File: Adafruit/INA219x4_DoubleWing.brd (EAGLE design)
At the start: 50.8 x 47 mm, 42 parts, among them J1 5mm, J3 5mm, J5 5mm, J7 5mm, U1 INA219BIDCNT, U2 INA219BIDCNT, U3 INA219BIDCNT, U4 INA219BIDCNT

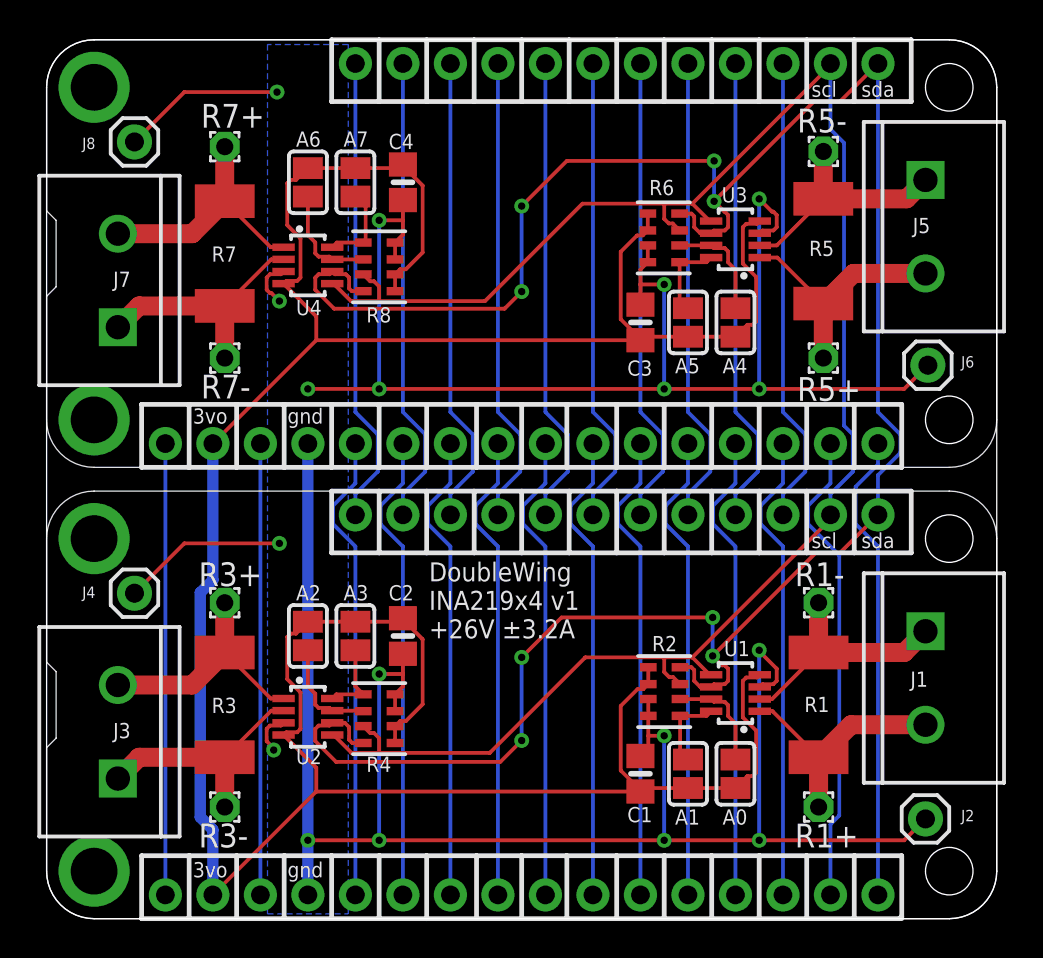
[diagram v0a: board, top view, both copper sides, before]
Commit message: DoubleWing INA219x4 v1.1: Better labels!
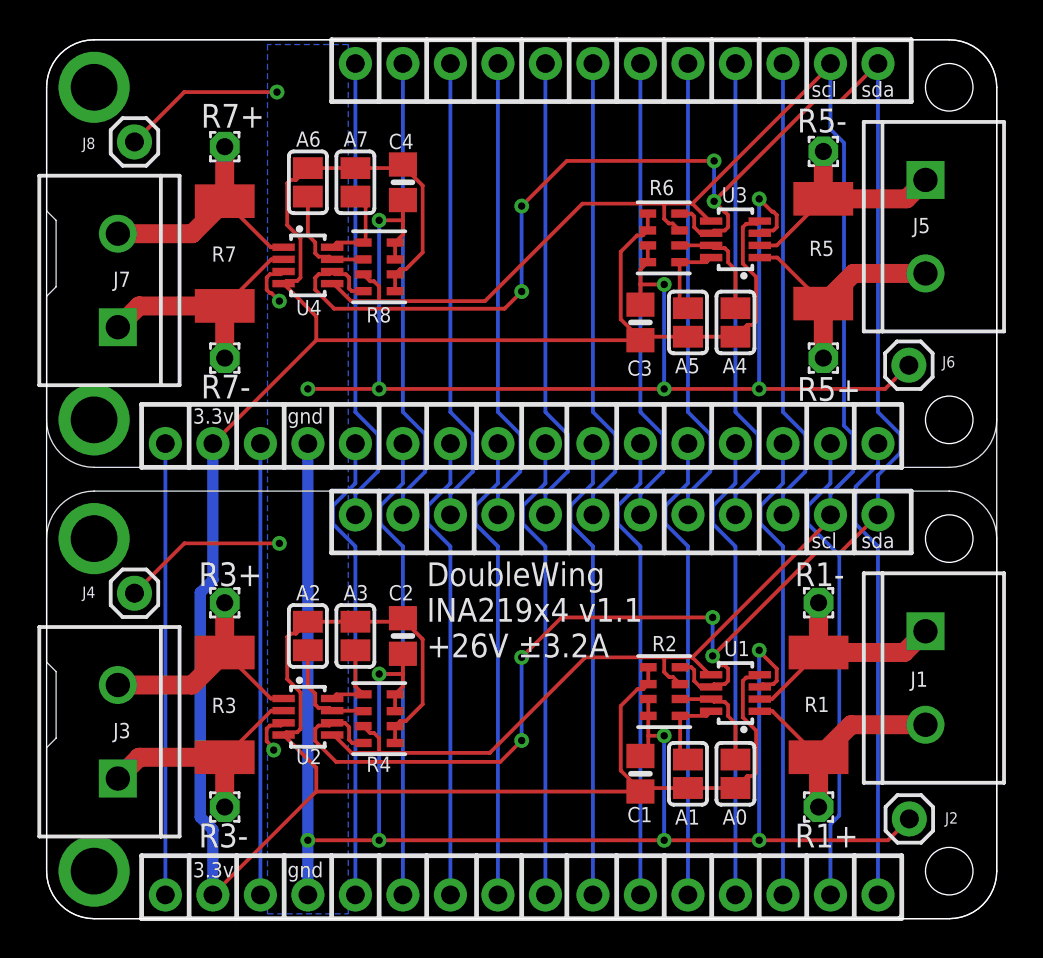
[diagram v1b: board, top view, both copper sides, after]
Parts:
- moved J6 1.02 mm to (46.1, 29.6)
- moved J2 0.86 mm to (46.1, 5.33)
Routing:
- net GND: track 187.1 -> 185.2 mm
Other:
- board text added: "+ve"
- board text added: "-ve"
- board text added: "3.3v"
- board text added: "DoubleWing INA219x4 v1.1"
- board text added: "DoubleWing INA219x4 v1.1 +26V ±3.2A"
- board text added: "VE: 0-26V Load: ±3.2A"
- board text added: "https://github.com/swooby/pcb/tree/master/Adafruit"
- board text added: "load"
- board text added: "parallel R1"
- board text added: "parallel R3"
- board text added: "parallel R5"
- board text added: "parallel R7"
- board text removed: "+26V ±3.2A"
- board text removed: "3vo"
- board text removed: "DoubleWing INA219x4 v1 +26V ±3.2A"
- board text removed: "INA219x4 DoubleWing v1"

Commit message: INA219x4 DoubleWing v2.0
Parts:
- removed A0, A1, A2, A3, A4, A5, A6, A7: (no value), microbuilder:SOLDERJUMPER_REFLOW_NOPASTE
- removed J4, J6, J8: (no value), SparkFun-Connectors:1X01
- removed R2, R4, R6, R8: 10K, microbuilder:RESPACK_4X0603
- removed R5: 0.1/1% (PT2512FK-070R1L), microbuilder:2512
- removed R5+, R5-, R7+, R7-: (no value), wirepad:1,6/0,9
- added J2#1, J2#2, J2#3: (no value), SparkFun-Connectors:1X01
- added JMPA0.1#1, JMPA0.1#2, JMPA0.1#3, JMPA0.1#4, JMPA0.2#1, JMPA0.2#2, JMPA0.2#3, JMPA0.2#4, JMPA1.1#1, JMPA1.1#2, JMPA1.1#3, JMPA1.1#4, JMPA1.2#1, JMPA1.2#2, JMPA1.2#3, JMPA1.2#4: 0R-JUMPD, pv_jump-0r-smd:C0R-JMP_NONE
- added R1#2: 0.1/1% (PT2512FK-070R1L), microbuilder:2512
- added R1+#1, R1+#2, R1-#1, R1-#2: (no value), wirepad:1,6/0,9
- added R2#1, R2#2, R2#3, R2#4: 10K, microbuilder:RESPACK_4X0603
- moved U3 33.5 mm to (15.1, 10.8), turned to 270 degrees
- moved U2 33.4 mm to (35.7, 36.2), turned to 90 degrees
- moved U1 31.5 mm to (15.1, 34.9), turned to 270 degrees
- moved U4 31.5 mm to (35.7, 12.1), turned to 90 degrees
- moved C2 30.5 mm to (37.0, 39.8), turned to 0 degrees
- moved C3 30.5 mm to (13.8, 7.24), turned to 180 degrees
- moved C4 29.8 mm to (37.0, 15.6), turned to 0 degrees
- moved C1 29.7 mm to (13.8, 31.4), turned to 180 degrees
- turned R1+#3 to 180 degrees
- turned R1-#3 to 180 degrees
- renumbered J1 to J1#4, J2 to J2#4, J3 to J1#3, J5 to J1#2, J7 to J1#1, R1 to R1#4, R1+ to R1+#4, R1- to R1-#4, R3 to R1#3, R3+ to R1+#3, R3- to R1-#3, R7 to R1#1
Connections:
- removed net N$16: A1.2, R2.1, U1.8
- removed net N$24: A5.2, R6.1, U3.8
- removed net N$25: A4.2, R6.2, U3.7
- removed net N$26: A0.2, R2.2, U1.7
- removed net N$27: A3.2, R4.1, U2.8
- removed net N$28: A2.2, R4.2, U2.7
- removed net N$29: A7.2, R8.1, U4.8
- removed net N$30: A6.2, R8.2, U4.7
- new net A0#1: JMPA0.1#1.2, JMPA0.2#1.2, R2#1.2, U1.7
- new net A0#2: JMPA0.1#2.2, JMPA0.2#2.2, R2#2.2, U2.7
- new net A0#3: JMPA0.1#3.2, JMPA0.2#3.2, R2#3.2, U3.7
- new net A0#4: JMPA0.1#4.2, JMPA0.2#4.2, R2#4.2, U4.7
- new net A1#1: JMPA1.1#1.2, JMPA1.2#1.2, R2#1.1, U1.8
- new net A1#2: JMPA1.1#2.2, JMPA1.2#2.2, R2#2.1, U2.8
- new net A1#3: JMPA1.1#3.2, JMPA1.2#3.2, R2#3.1, U3.8
- new net A1#4: JMPA1.1#4.2, JMPA1.2#4.2, R2#4.1, U4.8
- net 3.3V: now also JMPA0.1#1.1, JMPA0.1#2.1, JMPA0.1#3.1, JMPA0.1#4.1, JMPA1.1#1.1, JMPA1.1#2.1, JMPA1.1#3.1, JMPA1.1#4.1, R2#1.5, R2#1.6, R2#2.5, R2#2.6, R2#3.5, R2#3.6, R2#4.5, R2#4.6; no longer A0.1, A1.1, A2.1, A3.1, A4.1, A5.1, A6.1, A7.1, R2.5, R2.6, R4.5, R4.6, R6.5, R6.6, R8.5, R8.6
- net GND: now also J2#1.1, J2#2.1, J2#3.1, JMPA0.2#1.3, JMPA0.2#2.3, JMPA0.2#3.3, JMPA0.2#4.3, JMPA1.2#1.3, JMPA1.2#2.3, JMPA1.2#3.3, JMPA1.2#4.3, R2#1.7, R2#1.8, R2#2.7, R2#2.8, R2#3.7, R2#3.8, R2#4.7, R2#4.8; no longer J4.1, J6.1, J8.1, R2.7, R2.8, R4.7, R4.8, R6.7, R6.8, R8.7, R8.8
- net SCL: now also JMPA0.1#1.3, JMPA0.1#2.3, JMPA0.1#3.3, JMPA0.1#4.3, JMPA1.1#1.3, JMPA1.1#2.3, JMPA1.1#3.3, JMPA1.1#4.3, R2#1.4, R2#2.4, R2#3.4, R2#4.4; no longer R2.3, R4.3, R6.3, R8.3
- net SDA: now also JMPA0.2#1.1, JMPA0.2#2.1, JMPA0.2#3.1, JMPA0.2#4.1, JMPA1.2#1.1, JMPA1.2#2.1, JMPA1.2#3.1, JMPA1.2#4.1, R2#1.3, R2#2.3, R2#3.3, R2#4.3; no longer R2.4, R4.4, R6.4, R8.4
- net VIN1+: now also J1#1.2, R1#1.2, R1+#1.1; no longer J1#4.2, R1#4.2, R1+#4.1
- net VIN1-: now also J1#1.1, R1#1.1, R1-#1.1; no longer J1#4.1, R1#4.1, R1-#4.1
- net VIN2+: now also J1#2.2, R1#2.2, R1+#2.1; no longer J1#3.2, R1#3.2, R1+#3.1
- net VIN2-: now also J1#2.1, R1#2.1, R1-#2.1; no longer J1#3.1, R1#3.1, R1-#3.1
- net VIN3+: now also J1#3.2, R1#3.2, R1+#3.1; no longer J1#2.2, R5+.1, R5.2
- net VIN3-: now also J1#3.1, R1#3.1, R1-#3.1; no longer J1#2.1, R5-.1, R5.1
- net VIN4+: now also J1#4.2, R1#4.2, R1+#4.1; no longer J1#1.2, R1#1.2, R7+.1
- net VIN4-: now also J1#4.1, R1#4.1, R1-#4.1; no longer J1#1.1, R1#1.1, R7-.1
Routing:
- net SCL: track 100.3 -> 153.0 mm, vias 0 -> 12
- net SDA: track 127.1 -> 175.3 mm, vias 8 -> 12
- net 3.3V: track 165.9 -> 205.8 mm, vias 0 -> 14
- net GND: track 185.2 -> 199.6 mm, vias 18 -> 11
- net A1#1: track 0.00 -> 11.4 mm
- net A1#3: track 0.00 -> 11.4 mm
- net A1#4: track 0.00 -> 11.4 mm
- net A1#2: track 0.00 -> 11.4 mm
- net A0#2: track 0.00 -> 10.0 mm
- net A0#1: track 0.00 -> 9.97 mm
- net A0#3: track 0.00 -> 9.82 mm
- net A0#4: track 0.00 -> 9.82 mm
- net N$25: track 5.92 -> 0.00 mm
- net N$30: track 5.90 -> 0.00 mm
- net N$28: track 5.78 -> 0.00 mm
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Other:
- board text added: "A0"
- board text added: "A1"
- board text added: "A1 A0 ADDR GND GND 0x40 GND VS+ 0x41 GND SDA 0x42 GND SCL 0x43 VS+ GND 0x44 VS+ VS+ 0x45 VS+ SDA 0x46 VS+ SCL 0x47 SDA GND 0x48 SDA VS+ 0x49 SDA SDA 0x4A SDA SCL 0x4B SCL GND 0x4C SCL VS+ 0x4D SCL SDA 0x4E SCL SCL 0x4F"
- board text added: "DoubleWing INA219x4 v2.0"
- board text added: "GND"
- board text added: "SCL"
- board text added: "SDA"
- board text added: "VS+"
- board text added: "parallel R1#1"
- board text added: "parallel R1#2"
- board text added: "parallel R1#3"
- board text added: "parallel R1#4"
- board text removed: "DoubleWing INA219x4 v1.1"
- board text removed: "DoubleWing INA219x4 v1.1 +26V ±3.2A"
- board text removed: "parallel R1"
- board text removed: "parallel R3"
- board text removed: "parallel R5"
- board text removed: "parallel R7"
